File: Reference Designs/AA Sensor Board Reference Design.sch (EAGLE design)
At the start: 15 parts, among them M2 AETHERMESH_MODULEMEZZ-HOLES

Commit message: Final revisions to AA sensor reference design for production V1.0
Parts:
- removed TC2: TC2050-IDC, TagConnect:TC2050-IDC
- added R1, R5: 10K, 3. growflux:RESISTORR0402
- added TC1: DNP, TagConnect:TC2050-IDC
- JP1, JP2: value M01BAT_SLOT -> DNP
- JP3: value (none) -> DNP
- M2: value AETHERMESH_MODULEMEZZ-HOLES -> AETHERMESH_MODULEMEZZ-NOHOLES; device AetherConnectivity:AETHERMESH_MODULEMEZZ-HOLES -> AetherConnectivity:AETHERMESH_MODULEMEZZ-NOHOLES
- U$2: value M10X22X10_LOCK -> DNP
- renumbered U$1 to IC1
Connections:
- removed net RX: TC2.5
- removed net TX: TC2.7
- removed net VBAT: TC2.9
- net DIO7: now also R5.2
- net DIO8: now also R1.2
- net GND: now also IC1.ADDR, TC1.3, TC1.5, TC1.9; no longer TC2.10, TC2.3
- net RESET: now also TC1.10; no longer TC2.2
- net TCK: now also TC1.4; no longer TC2.8
- net TDI: now also TC1.8; no longer TC2.4
- net TDO: now also TC1.6; no longer TC2.6
- net TMS: now also TC1.2; no longer TC2.1
- net VCC: now also R1.1, R5.1, TC1.1

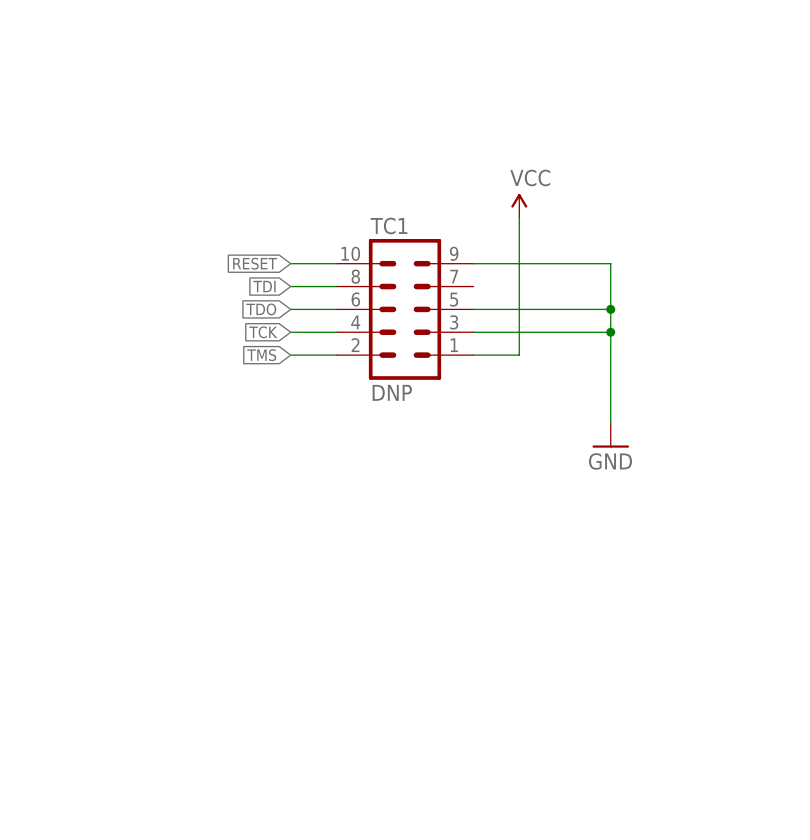
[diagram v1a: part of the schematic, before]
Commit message: Updated reference designs and test boards with latest XDS programmer tag connect header
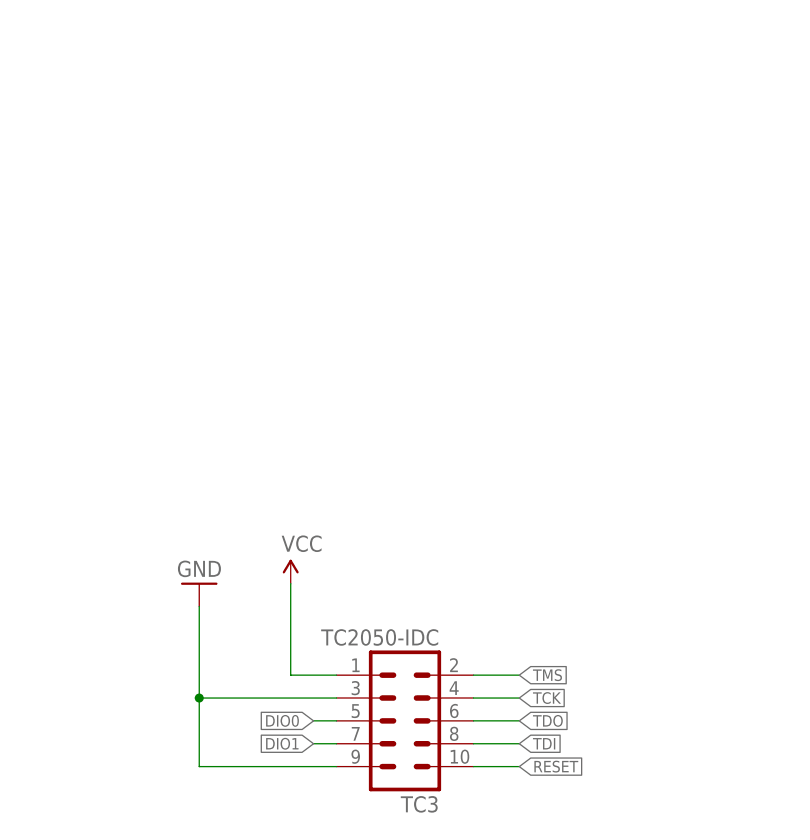
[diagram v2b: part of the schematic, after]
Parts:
- removed TC1: DNP, TagConnect:TC2050-IDC
- added TC3: TC2050-IDC, TagConnect:TC2050-IDC
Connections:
- net DIO0: now also TC3.5
- net DIO1: now also TC3.7
- net GND: now also TC3.3, TC3.9; no longer TC1.3, TC1.5, TC1.9
- net RESET: now also TC3.10; no longer TC1.10
- net TCK: now also TC3.4; no longer TC1.4
- net TDI: now also TC3.8; no longer TC1.8
- net TDO: now also TC3.6; no longer TC1.6
- net TMS: now also TC3.2; no longer TC1.2
- net VCC: now also TC3.1; no longer TC1.1
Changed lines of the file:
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@@
 <?xml version="1.0" encoding="utf-8"?>
 <!DOCTYPE eagle SYSTEM "eagle.dtd">
-<eagle version="8.6.0">
+<eagle version="9.0.0">
 <drawing>
 <settings>
@@
 <part name="SUPPLY2" library="SparkFun-Aesthetics" deviceset="VCC" device=""/>
 <part name="GND11" library="3. growflux" library_urn="urn:adsk.eagle:library:207379" deviceset="GND" device=""/>
-<part name="TC1" library="TagConnect" deviceset="TC2050-IDC" device="" value="DNP"/>
-<part name="GND15" library="SparkFun-Aesthetics" deviceset="GND" device=""/>
-<part name="SUPPLY7" library="SparkFun-Aesthetics" deviceset="VCC" device=""/>
 <part name="GND3" library="3. growflux" library_urn="urn:adsk.eagle:library:207379" deviceset="GND" device=""/>
 <part name="R1" library="3. growflux" deviceset="RESISTOR" device="R0402" package3d_urn="urn:adsk.eagle:package:208129/1" value="10K">
@@
 <part name="SUPPLY8" library="SparkFun-Aesthetics" deviceset="VCC" device=""/>
 <part name="SUPPLY9" library="SparkFun-Aesthetics" deviceset="VCC" device=""/>
+<part name="TC3" library="TagConnect" deviceset="TC2050-IDC" device=""/>
+<part name="GND5" library="SparkFun-Aesthetics" deviceset="GND" device=""/>
+<part name="SUPPLY10" library="SparkFun-Aesthetics" deviceset="VCC" device=""/>
 </parts>
 <sheets>
@@
 <instance part="SUPPLY2" gate="G$1" x="-15.24" y="104.14"/>
 <instance part="GND11" gate="1" x="-25.4" y="68.58"/>
-<instance part="TC1" gate="A" x="152.4" y="33.02"/>
-<instance part="GND15" gate="1" x="175.26" y="17.78"/>
-<instance part="SUPPLY7" gate="G$1" x="165.1" y="43.18"/>
 <instance part="GND3" gate="1" x="198.12" y="71.12"/>
 <instance part="R1" gate="G$1" x="193.04" y="106.68" rot="R270">
@@
 <instance part="SUPPLY8" gate="G$1" x="193.04" y="114.3"/>
 <instance part="SUPPLY9" gate="G$1" x="200.66" y="114.3"/>
+<instance part="TC3" gate="A" x="152.4" y="-12.7" rot="R180"/>
+<instance part="GND5" gate="1" x="129.54" y="2.54" rot="R180"/>
+<instance part="SUPPLY10" gate="G$1" x="139.7" y="2.54"/>
 </instances>
 <busses>
@@
 </segment>
 <segment>
-<pinref part="TC1" gate="A" pin="3"/>
-<wire x1="160.02" y1="30.48" x2="175.26" y2="30.48" width="0.1524" layer="91"/>
-<wire x1="175.26" y1="30.48" x2="175.26" y2="20.32" width="0.1524" layer="91"/>
-<pinref part="GND15" gate="1" pin="GND"/>
-<pinref part="TC1" gate="A" pin="5"/>
-<wire x1="160.02" y1="33.02" x2="175.26" y2="33.02" width="0.1524" layer="91"/>
-<wire x1="175.26" y1="33.02" x2="175.26" y2="30.48" width="0.1524" layer="91"/>
-<junction x="175.26" y="30.48"/>
-<pinref part="TC1" gate="A" pin="9"/>
-<wire x1="160.02" y1="38.1" x2="175.26" y2="38.1" width="0.1524" layer="91"/>
-<wire x1="175.26" y1="38.1" x2="175.26" y2="33.02" width="0.1524" layer="91"/>
-<junction x="175.26" y="33.02"/>
-</segment>
-<segment>
 <pinref part="IC1" gate="G$1" pin="ADDR"/>
 <wire x1="190.5" y1="88.9" x2="198.12" y2="88.9" width="0.1524" layer="91"/>
 <wire x1="198.12" y1="88.9" x2="198.12" y2="73.66" width="0.1524" layer="91"/>
 <pinref part="GND3" gate="1" pin="GND"/>
+</segment>
+<segment>
+<pinref part="TC3" gate="A" pin="3"/>
+<wire x1="144.78" y1="-10.16" x2="129.54" y2="-10.16" width="0.1524" layer="91"/>
+<wire x1="129.54" y1="-10.16" x2="129.54" y2="0" width="0.1524" layer="91"/>
+<pinref part="GND5" gate="1" pin="GND"/>
+<junction x="129.54" y="-10.16"/>
+<pinref part="TC3" gate="A" pin="9"/>
+<wire x1="144.78" y1="-17.78" x2="129.54" y2="-17.78" width="0.1524" layer="91"/>
+<wire x1="129.54" y1="-17.78" x2="129.54" y2="-10.16" width="0.1524" layer="91"/>
 </segment>
 </net>
@@
 </segment>
 <segment>
-<pinref part="TC1" gate="A" pin="1"/>
-<wire x1="165.1" y1="27.94" x2="160.02" y2="27.94" width="0.1524" layer="91"/>
-<pinref part="SUPPLY7" gate="G$1" pin="VCC"/>
-<wire x1="165.1" y1="43.18" x2="165.1" y2="27.94" width="0.1524" layer="91"/>
-</segment>
-<segment>
 <pinref part="R1" gate="G$1" pin="1"/>
 <pinref part="SUPPLY8" gate="G$1" pin="VCC"/>
@@
 <wire x1="200.66" y1="111.76" x2="200.66" y2="114.3" width="0.1524" layer="91"/>
 </segment>
+<segment>
+<pinref part="TC3" gate="A" pin="1"/>
+<wire x1="139.7" y1="-7.62" x2="144.78" y2="-7.62" width="0.1524" layer="91"/>
+<pinref part="SUPPLY10" gate="G$1" pin="VCC"/>
+<wire x1="139.7" y1="2.54" x2="139.7" y2="-7.62" width="0.1524" layer="91"/>
+</segment>
 </net>
 <net name="DIO2" class="0">
@@
 <label x="-15.24" y="88.9" size="1.27" layer="95" rot="R180" xref="yes"/>
 </segment>
+<segment>
+<pinref part="TC3" gate="A" pin="5"/>
+<wire x1="142.24" y1="-12.7" x2="144.78" y2="-12.7" width="0.1524" layer="91"/>
+<label x="142.24" y="-12.7" size="1.27" layer="95" rot="R180" xref="yes"/>
+</segment>
 </net>
 <net name="DIO1" class="0">
@@
 <wire x1="-15.24" y1="86.36" x2="-12.7" y2="86.36" width="0.1524" layer="91"/>
 <label x="-15.24" y="86.36" size="1.27" layer="95" rot="R180" xref="yes"/>
+</segment>
+<segment>
+<pinref part="TC3" gate="A" pin="7"/>
+<wire x1="142.24" y1="-15.24" x2="144.78" y2="-15.24" width="0.1524" layer="91"/>
+<label x="142.24" y="-15.24" size="1.27" layer="95" rot="R180" xref="yes"/>
 </segment>
 </net>
@@
 </segment>
 <segment>
-<pinref part="TC1" gate="A" pin="10"/>
-<wire x1="144.78" y1="38.1" x2="139.7" y2="38.1" width="0.1524" layer="91"/>
-<label x="139.7" y="38.1" size="1.27" layer="95" rot="R180" xref="yes"/>
+<pinref part="TC3" gate="A" pin="10"/>
+<wire x1="160.02" y1="-17.78" x2="165.1" y2="-17.78" width="0.1524" layer="91"/>
+<label x="165.1" y="-17.78" size="1.27" layer="95" xref="yes"/>
 </segment>
 </net>
@@
 </segment>
 <segment>
-<pinref part="TC1" gate="A" pin="8"/>
-<wire x1="139.7" y1="35.56" x2="144.78" y2="35.56" width="0.1524" layer="91"/>
-<label x="139.7" y="35.56" size="1.27" layer="95" rot="R180" xref="yes"/>
+<pinref part="TC3" gate="A" pin="8"/>
+<wire x1="165.1" y1="-15.24" x2="160.02" y2="-15.24" width="0.1524" layer="91"/>
+<label x="165.1" y="-15.24" size="1.27" layer="95" xref="yes"/>
 </segment>
 </net>
@@
 </segment>
 <segment>
-<pinref part="TC1" gate="A" pin="6"/>
-<wire x1="139.7" y1="33.02" x2="144.78" y2="33.02" width="0.1524" layer="91"/>
-<label x="139.7" y="33.02" size="1.27" layer="95" rot="R180" xref="yes"/>
+<pinref part="TC3" gate="A" pin="6"/>
+<wire x1="165.1" y1="-12.7" x2="160.02" y2="-12.7" width="0.1524" layer="91"/>
+<label x="165.1" y="-12.7" size="1.27" layer="95" xref="yes"/>
 </segment>
 </net>
@@
 </segment>
 <segment>
-<pinref part="TC1" gate="A" pin="4"/>
-<wire x1="139.7" y1="30.48" x2="144.78" y2="30.48" width="0.1524" layer="91"/>
-<label x="139.7" y="30.48" size="1.27" layer="95" rot="R180" xref="yes"/>
+<pinref part="TC3" gate="A" pin="4"/>
+<wire x1="165.1" y1="-10.16" x2="160.02" y2="-10.16" width="0.1524" layer="91"/>
+<label x="165.1" y="-10.16" size="1.27" layer="95" xref="yes"/>
 </segment>
 </net>
@@
 </segment>
 <segment>
-<pinref part="TC1" gate="A" pin="2"/>
-<wire x1="139.7" y1="27.94" x2="144.78" y2="27.94" width="0.1524" layer="91"/>
-<label x="139.7" y="27.94" size="1.27" layer="95" rot="R180" xref="yes"/>
-</segment>
-</net>
+<pinref part="TC3" gate="A" pin="2"/>
+<wire x1="165.1" y1="-7.62" x2="160.02" y2="-7.62" width="0.1524" layer="91"/>
+<label x="165.1" y="-7.62" size="1.27" layer="95" xref="yes"/>
+</segment>
+</net>
